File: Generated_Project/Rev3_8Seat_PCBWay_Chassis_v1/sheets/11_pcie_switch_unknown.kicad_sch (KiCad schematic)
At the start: 0 parts

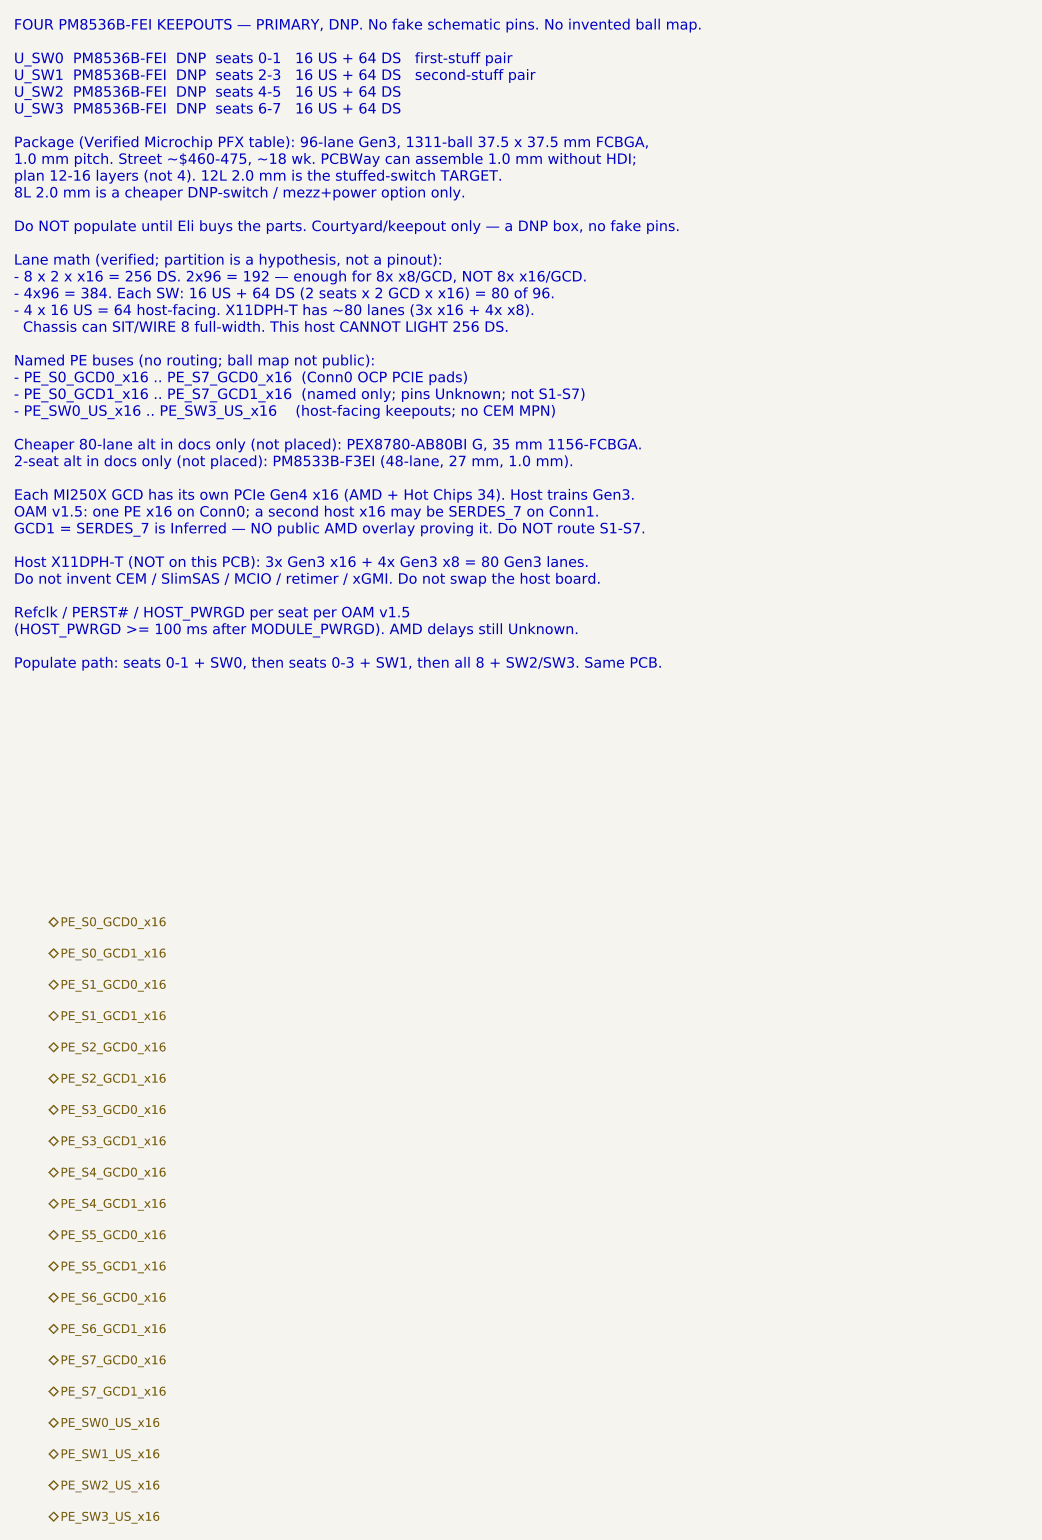
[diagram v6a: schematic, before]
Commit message: Retarget Rev3 first article to seats 0-1 GCD0 x16 (2-module path).
Same 8-seat PCB. Without overlay, 2x MI250X means two modules can sit
and at most GCD0 on each can be named toward the host keepout (2 GCDs),
not 2x full-width (4 GCDs). Conn0 OCP PCIE_* is the only legal host PE.
No CEM/MCIO MPN. Do not energize P48V.

Co-authored-by: zivzancoeli-commits <zivzancoeli-commits@users.noreply.github.com>
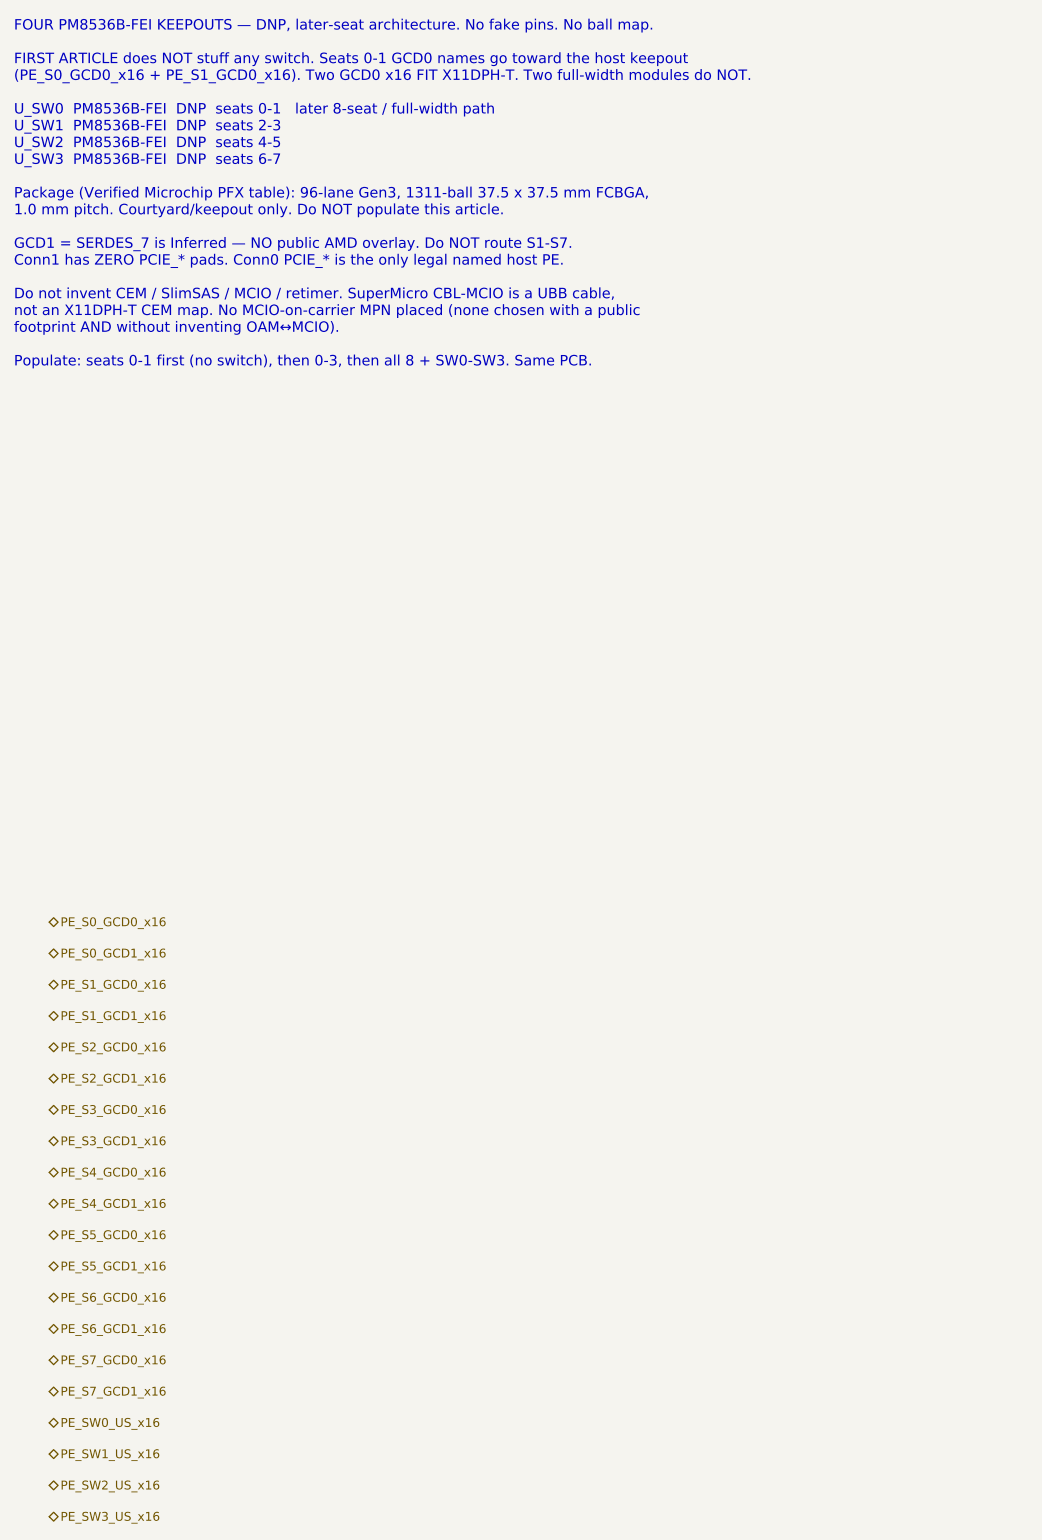
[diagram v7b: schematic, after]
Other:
- note added: "FOUR PM8536B-FEI KEEPOUTS — DNP, later-seat architecture. No fake pins. No ball map. FIRST ARTICLE does NOT stuff any switch. Seats 0-1 GCD0 names go toward the host keepout (PE_S0_GCD0_x16 + PE_S1_GCD0_x16). Two GCD0 x16 FIT X11DPH-T. Two full-width modules do NOT. U_SW0 PM8536B-FEI DNP seats 0-1 later 8-seat / full-width path U_SW1 PM8536B-FEI DNP seats 2-3 U_SW2 PM8536B-FEI DNP seats 4-5 U_SW3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"
- note removed: "FOUR PM8536B-FEI KEEPOUTS — PRIMARY, DNP. No fake schematic pins. No invented ball map. U_SW0 PM8536B-FEI DNP seats 0-1 16 US + 64 DS first-stuff pair U_SW1 PM8536B-FEI DNP seats 2-3 16 US + 64 DS second-stuff pair U_SW2 PM8536B-FEI DNP seats 4-5 16 US + 64 DS U_SW3 PM8536B-FEI DNP seats 6-7 16 US + 64 DS Package (Verified Microchip PFX table): 96-lane Gen3, 1311-ball 37.5 x 37.5 mm FCBGA, 1.0 mm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"
- title: PM8536B-FEI DNP x4 PRIMARY (keepout only) -> PM8536B-FEI DNP x4 (later path; not stuffed for 2-mod)
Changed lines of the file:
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@@
 	(paper "A3")
 	(title_block
-		(title "PM8536B-FEI DNP x4 PRIMARY (keepout only)")
+		(title "PM8536B-FEI DNP x4 (later path; not stuffed for 2-mod)")
 		(date "2026-08-22")
 		(rev "Rev3_8Seat_PCBWay_v1")
@@
         (comment 4 "r2.0 UNUSABLE. P3V3=Conn0 C1/C2. 12L 2.0mm stuffed-switch TARGET. 4x PM8536 DNP. Star-fed P48V.")
 	)
-	(text "FOUR PM8536B-FEI KEEPOUTS — PRIMARY, DNP. No fake schematic pins. No invented ball map.\n\nU_SW0  PM8536B-FEI  DNP  seats 0-1   16 US + 64 DS   first-stuff pair\nU_SW1  PM8536B-FEI  DNP  seats 2-3   16 US + 64 DS   second-stuff pair\nU_SW2  PM8536B-FEI  DNP  seats 4-5   16 US + 64 DS\nU_SW3  PM8536B-FEI  DNP  seats 6-7   16 US + 64 DS\n\nPackage (Verified Microchip PFX table): 96-lane Gen3, 1311-ball 37.5 x 37.5 mm FCBGA,\n1.0 mm pitch. Street ~$460-475, ~18 wk. PCBWay can assemble 1.0 mm without HDI;\nplan 12-16 layers (not 4). 12L 2.0 mm is the stuffed-switch TARGET.\n8L 2.0 mm is a cheaper DNP-switch / mezz+power option only.\n\nDo NOT populate until Eli buys the parts. Courtyard/keepout only — a DNP box, no fake pins.\n\nLane math (verified; partition is a hypothesis, not a pinout):\n- 8 x 2 x x16 = 256 DS. 2x96 = 192 — enough for 8x x8/GCD, NOT 8x x16/GCD.\n- 4x96 = 384. Each SW: 16 US + 64 DS (2 seats x 2 GCD x x16) = 80 of 96.\n- 4 x 16 US = 64 host-facing. X11DPH-T has ~80 lanes (3x x16 + 4x x8).\n  Chassis can SIT/WIRE 8 full-width. This host CANNOT LIGHT 256 DS.\n\nNamed PE buses (no routing; ball map not public):\n- PE_S0_GCD0_x16 .. PE_S7_GCD0_x16  (Conn0 OCP PCIE pads)\n- PE_S0_GCD1_x16 .. PE_S7_GCD1_x16  (named only; pins Unknown; not S1-S7)\n- PE_SW0_US_x16 .. PE_SW3_US_x16    (host-facing keepouts; no CEM MPN)\n\nCheaper 80-lane alt in docs only (not placed): PEX8780-AB80BI G, 35 mm 1156-FCBGA.\n2-seat alt in docs only (not placed): PM8533B-F3EI (48-lane, 27 mm, 1.0 mm).\n\nEach MI250X GCD has its own PCIe Gen4 x16 (AMD + Hot Chips 34). Host trains Gen3.\nOAM v1.5: one PE x16 on Conn0; a second host x16 may be SERDES_7 on Conn1.\nGCD1 = SERDES_7 is Inferred — NO public AMD overlay proving it. Do NOT route S1-S7.\n\nHost X11DPH-T (NOT on this PCB): 3x Gen3 x16 + 4x Gen3 x8 = 80 Gen3 lanes.\nDo not invent CEM / SlimSAS / MCIO / retimer / xGMI. Do not swap the host board.\n\nRefclk / PERST# / HOST_PWRGD per seat per OAM v1.5\n(HOST_PWRGD >= 100 ms after MODULE_PWRGD). AMD delays still Unknown.\n\nPopulate path: seats 0-1 + SW0, then seats 0-3 + SW1, then all 8 + SW2/SW3. Same PCB.\n"
+	(text "FOUR PM8536B-FEI KEEPOUTS — DNP, later-seat architecture. No fake pins. No ball map.\n\nFIRST ARTICLE does NOT stuff any switch. Seats 0-1 GCD0 names go toward the host keepout\n(PE_S0_GCD0_x16 + PE_S1_GCD0_x16). Two GCD0 x16 FIT X11DPH-T. Two full-width modules do NOT.\n\nU_SW0  PM8536B-FEI  DNP  seats 0-1   later 8-seat / full-width path\nU_SW1  PM8536B-FEI  DNP  seats 2-3\nU_SW2  PM8536B-FEI  DNP  seats 4-5\nU_SW3  PM8536B-FEI  DNP  seats 6-7\n\nPackage (Verified Microchip PFX table): 96-lane Gen3, 1311-ball 37.5 x 37.5 mm FCBGA,\n1.0 mm pitch. Courtyard/keepout only. Do NOT populate this article.\n\nGCD1 = SERDES_7 is Inferred — NO public AMD overlay. Do NOT route S1-S7.\nConn1 has ZERO PCIE_* pads. Conn0 PCIE_* is the only legal named host PE.\n\nDo not invent CEM / SlimSAS / MCIO / retimer. SuperMicro CBL-MCIO is a UBB cable,\nnot an X11DPH-T CEM map. No MCIO-on-carrier MPN placed (none chosen with a public\nfootprint AND without inventing OAM↔MCIO).\n\nPopulate: seats 0-1 first (no switch), then 0-3, then all 8 + SW0-SW3. Same PCB.\n"
 		(exclude_from_sim no)
 		(at 20.32 20.32 0)

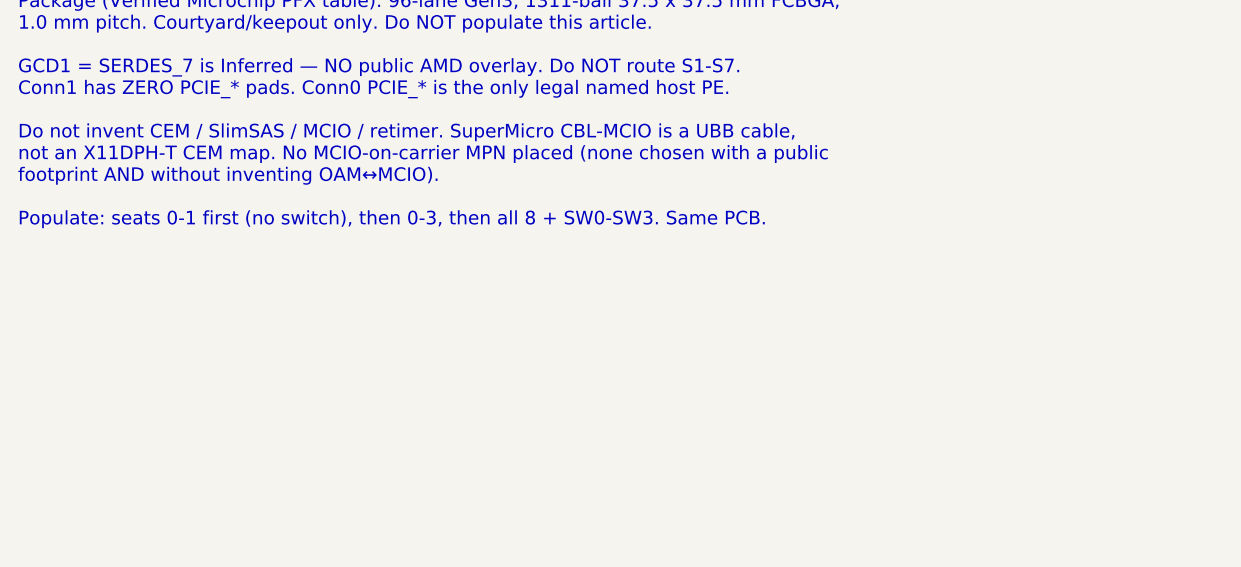
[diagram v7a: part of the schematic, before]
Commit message: Document an 8x full-width chassis CONCEPT (ideas only, not fab).
Sibling folder plus STATUS pointer. Comments-layer KiCad notes say
CONCEPT / DO NOT FABRICATE. No overlay, ball map, CEM/MCIO, r2.0, or
S1-S7 assignment. X11DPH-T cannot light 256 DS. Do not energize.
Do not upload to PCBWay.

Co-authored-by: zivzancoeli-commits <zivzancoeli-commits@users.noreply.github.com>
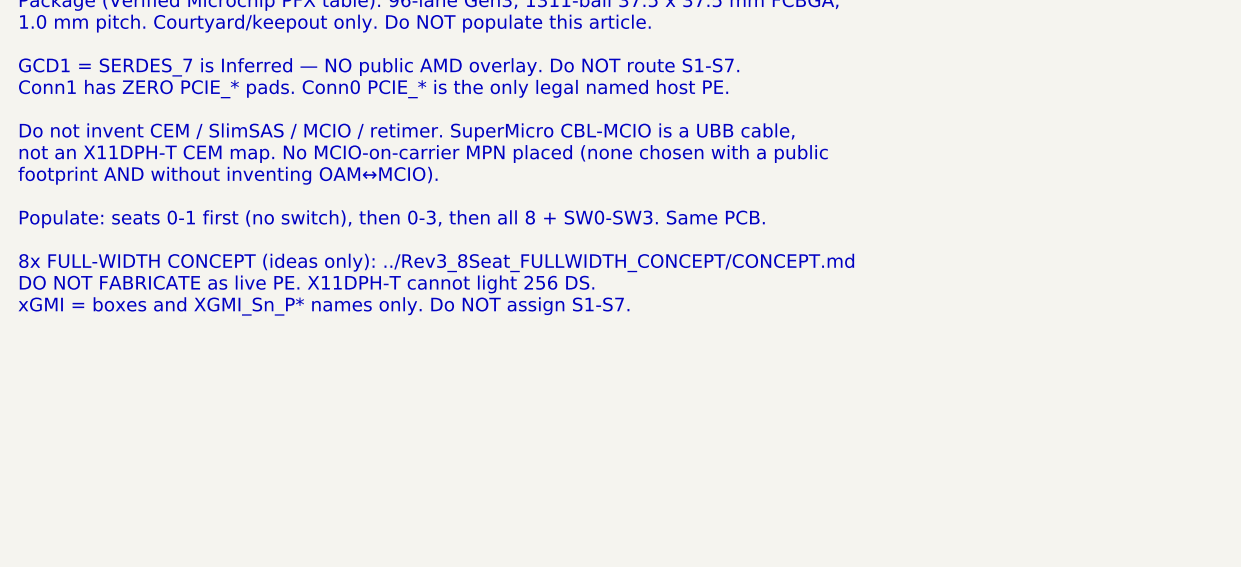
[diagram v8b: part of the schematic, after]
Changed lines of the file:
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@@
         (comment 4 "r2.0 UNUSABLE. P3V3=Conn0 C1/C2. 12L 2.0mm stuffed-switch TARGET. 4x PM8536 DNP. Star-fed P48V.")
 	)
-	(text "FOUR PM8536B-FEI KEEPOUTS — DNP, later-seat architecture. No fake pins. No ball map.\n\nFIRST ARTICLE does NOT stuff any switch. Seats 0-1 GCD0 names go toward the host keepout\n(PE_S0_GCD0_x16 + PE_S1_GCD0_x16). Two GCD0 x16 FIT X11DPH-T. Two full-width modules do NOT.\n\nU_SW0  PM8536B-FEI  DNP  seats 0-1   later 8-seat / full-width path\nU_SW1  PM8536B-FEI  DNP  seats 2-3\nU_SW2  PM8536B-FEI  DNP  seats 4-5\nU_SW3  PM8536B-FEI  DNP  seats 6-7\n\nPackage (Verified Microchip PFX table): 96-lane Gen3, 1311-ball 37.5 x 37.5 mm FCBGA,\n1.0 mm pitch. Courtyard/keepout only. Do NOT populate this article.\n\nGCD1 = SERDES_7 is Inferred — NO public AMD overlay. Do NOT route S1-S7.\nConn1 has ZERO PCIE_* pads. Conn0 PCIE_* is the only legal named host PE.\n\nDo not invent CEM / SlimSAS / MCIO / retimer. SuperMicro CBL-MCIO is a UBB cable,\nnot an X11DPH-T CEM map. No MCIO-on-carrier MPN placed (none chosen with a public\nfootprint AND without inventing OAM↔MCIO).\n\nPopulate: seats 0-1 first (no switch), then 0-3, then all 8 + SW0-SW3. Same PCB.\n"
+	(text "FOUR PM8536B-FEI KEEPOUTS — DNP, later-seat architecture. No fake pins. No ball map.\n\nFIRST ARTICLE does NOT stuff any switch. Seats 0-1 GCD0 names go toward the host keepout\n(PE_S0_GCD0_x16 + PE_S1_GCD0_x16). Two GCD0 x16 FIT X11DPH-T. Two full-width modules do NOT.\n\nU_SW0  PM8536B-FEI  DNP  seats 0-1   later 8-seat / full-width path\nU_SW1  PM8536B-FEI  DNP  seats 2-3\nU_SW2  PM8536B-FEI  DNP  seats 4-5\nU_SW3  PM8536B-FEI  DNP  seats 6-7\n\nPackage (Verified Microchip PFX table): 96-lane Gen3, 1311-ball 37.5 x 37.5 mm FCBGA,\n1.0 mm pitch. Courtyard/keepout only. Do NOT populate this article.\n\nGCD1 = SERDES_7 is Inferred — NO public AMD overlay. Do NOT route S1-S7.\nConn1 has ZERO PCIE_* pads. Conn0 PCIE_* is the only legal named host PE.\n\nDo not invent CEM / SlimSAS / MCIO / retimer. SuperMicro CBL-MCIO is a UBB cable,\nnot an X11DPH-T CEM map. No MCIO-on-carrier MPN placed (none chosen with a public\nfootprint AND without inventing OAM↔MCIO).\n\nPopulate: seats 0-1 first (no switch), then 0-3, then all 8 + SW0-SW3. Same PCB.\n\n8x FULL-WIDTH CONCEPT (ideas only): ../Rev3_8Seat_FULLWIDTH_CONCEPT/CONCEPT.md\nDO NOT FABRICATE as live PE. X11DPH-T cannot light 256 DS.\nxGMI = boxes and XGMI_Sn_P* names only. Do NOT assign S1-S7.\n"
 		(exclude_from_sim no)
 		(at 20.32 20.32 0)
